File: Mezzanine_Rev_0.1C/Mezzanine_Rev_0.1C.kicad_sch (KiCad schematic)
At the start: 51 parts, among them J1 QBUS_DWK_64Pin_MBT, J2 DIP20 Header, J3 DIP20 Header, J4 IDC-64M, J5 IDC-16M, J6 IDC-20M, J7 Conn_01x03_Pin, J8 Conn_01x07_Pin, U1 1533LI1, U10 74LS07, U11 74LS74, U2 1533TM2, U3 1533LA8, U4 CD74HCT4067M, U5 1533LE4, U6 1533AP6, U7 1533AP6, U8 74LS07, U9 74LS07

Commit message: Mezzanine: Board layout
Completed layout, to be verified and refined if needed.
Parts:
- removed J8: Conn_01x07_Pin, Connector_PinHeader_2.54mm:PinHeader_1x06_P2.54mm_Horizontal, symbol Connector:Conn_01x07_Pin
- added C11, C12, C13, C14, C15, C16, C17, C18, C19, C20: 0.1uF, Capacitor_THT:C_Disc_D6.0mm_W2.5mm_P5.00mm, symbol Device:C
- added unit 2 of DD1
- added unit 2 of DD10
- added unit 2 of DD2
- added unit 2 of DD3
- added unit 2 of DD4
- added unit 2 of DD6
- added unit 2 of DD7
- added unit 2 of DD8
- added unit 2 of DD9
- added J8: Conn_01x16_Pin, Connector_PinHeader_2.54mm:PinHeader_1x16_P2.54mm_Horizontal, symbol Connector:Conn_01x16_Pin
- added R7: 2.2K, Resistor_THT:R_Axial_DIN0204_L3.6mm_D1.6mm_P7.62mm_Horizontal, symbol Device:R
- added unit 7 of U10
- added unit 3 of U11
- added unit 1 of U8
- added unit 2 of U8
- added unit 4 of U8
- added unit 5 of U8
- added unit 6 of U8
- added unit 7 of U8
- added unit 3 of U9
- R6: footprint Resistor_THT:R_Axial_DIN0204_L3.6mm_D1.6mm_P7.62mm_Horizontal -> Resistor_THT:R_Axial_DIN0207_L6.3mm_D2.5mm_P7.62mm_Horizontal
- U4: footprint Package_SO:SOIC-24W_7.5x15.4mm_P1.27mm -> Package_DIP:DIP-24_W15.24mm
- renumbered D6 to DD6, D7 to DD7
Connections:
- net BDCOK: now also RN3.3 (R2); no longer RN3.2 (R1)
- net BPOK: now also RN3.2 (R1); no longer RN2.10 (R9)
- net CPU_DIN: now also J8.12 (Pin_12)
- net DOUT: now also J8.13 (Pin_13)
- net GND: now also C11.2, C12.2, C13.2, C14.2, C15.2, C16.2, C17.2, C18.2, C19.2, C20.2, DD1.8 (GND), DD10.8 (GND), DD2.8 (GND), DD3.8 (GND), DD4.8 (GND), DD6.8 (GND), DD7.8 (GND), DD8.8 (GND), DD9.8 (GND), U10.7 (GND), U11.7 (GND), U8.7 (GND); no longer DD1.8 (GND), DD10.8 (GND), DD2.8 (GND), DD3.8 (GND), DD4.8 (GND), DD6.8 (GND), DD7.8 (GND), DD8.8 (GND), DD9.8 (GND), U10.7 (GND), U8.7 (GND)
- net SEL1: now also J8.14 (Pin_14)
- net SRUN: now also RN4.4 (R3); no longer RN4.8 (R7)
- net SSpare7: now also RN2.8 (R7); no longer RN2.7 (R6)
- net SYSRAM: now also J8.15 (Pin_15)
- net VCC: now also C11.1, C12.1, C13.1, C14.1, C15.1, C16.1, C17.1, C18.1, C19.1, C20.1, DD1.16 (VCC), DD10.16 (VCC), DD2.16 (VCC), DD3.16 (VCC), DD4.16 (VCC), DD6.16 (VCC), DD7.16 (VCC), DD8.16 (VCC), DD9.16 (VCC), R7.1, U10.14 (VCC), U11.14 (VCC), U8.14 (VCC); no longer DD1.16 (VCC), DD10.16 (VCC), DD2.16 (VCC), DD3.16 (VCC), DD4.16 (VCC), DD6.16 (VCC), DD7.16 (VCC), DD8.16 (VCC), DD9.16 (VCC), U10.14 (VCC), U8.14 (VCC)
- net ~{A0}: now also U8.9; no longer U8.1
- net ~{A10}: now also U9.13; no longer U9.11
- net ~{A11}: now also U9.1; no longer U9.13
- net ~{A12}: now also U10.9; no longer U10.1
- net ~{A13}: now also U10.5; no longer U10.3
- net ~{A14}: now also U10.11; no longer U10.5
- net ~{A15}: now also U10.3; no longer U10.9
- net ~{A1}: now also U8.5; no longer U8.3
- net ~{A2}: now also U8.11; no longer U8.5
- net ~{A3}: now also U8.3; no longer U8.9
- net ~{A4}: now also U8.13; no longer U8.11
- net ~{A5}: now also U8.1; no longer U8.13
- net ~{A6}: now also U9.9; no longer U9.1
- net ~{A7}: now also U9.5; no longer U9.3
- net ~{A8}: now also U9.11; no longer U9.5
- net ~{A9}: now also U9.3; no longer U9.9
- net ~{BBS7}: now also RN3.10 (R9); no longer RN3.8 (R7)
- net ~{BDAL0}: now also RN3.5 (R4); no longer RN3.4 (R3)
- net ~{BDAL10}: now also RN1.8 (R7); no longer RN1.7 (R6)
- net ~{BDAL11}: now also RN1.6 (R5)
- net ~{BDAL1}: now also RN3.4 (R3); no longer RN3.3 (R2)
- net ~{BDAL2}: now also RN2.9 (R8); no longer RN2.8 (R7)
- net ~{BDAL3}: now also RN2.7 (R6); no longer RN2.6 (R5)
- net ~{BDAL4}: now also RN2.6 (R5); no longer RN2.5 (R4)
- net ~{BDAL5}: now also RN2.5 (R4); no longer RN2.4 (R3)
- net ~{BDAL6}: now also RN2.4 (R3); no longer RN2.3 (R2)
- net ~{BDAL7}: now also RN2.3 (R2); no longer RN2.2 (R1)
- net ~{BDAL8}: now also RN2.2 (R1); no longer RN1.10 (R9)
- net ~{BDAL9}: now also RN1.9 (R8); no longer RN1.8 (R7)
- net ~{BDIN}: now also RN4.3 (R2); no longer RN4.7 (R6)
- net ~{BDMGI}: now also RN3.8 (R7); no longer RN3.7 (R6)
- net ~{BDMGO}: now also RN3.7 (R6); no longer RN3.6 (R5)
- net ~{BDMR}: now also RN4.10 (R9); no longer RN4.2 (R1)
- net ~{BDOUT}: now also R7.2; no longer RN4.10 (R9)
- net ~{BEVNT}: now also RN1.7 (R6); no longer RN1.6 (R5)
- net ~{BIAKI}: now also RN4.8 (R7); no longer RN4.3 (R2)
- net ~{BIAKO}: now also RN4.9 (R8); no longer RN3.10 (R9)
- net ~{BINIT}: now also RN3.6 (R5); no longer RN3.5 (R4)
- net ~{BIRQ3}: now also RN2.10 (R9); no longer RN2.9 (R8)
- net ~{BIRQ4}: now also RN4.7 (R6); no longer RN4.4 (R3)
- net ~{BRPLY}: now also RN4.2 (R1); no longer RN4.9 (R8)
- net ~{BSACK}: now also RN1.10 (R9); no longer RN1.9 (R8)
- net ~{BSYNC}: now also RN4.5 (R4); no longer RN4.6 (R5)
- net ~{BWTBT}: now also RN4.6 (R5); no longer RN4.5 (R4)
- net ~{CPU_DIN}: now also J8.11 (Pin_11)
- net ~{CPU_DOUT}: now also J8.8 (Pin_8)
- net ~{CPU_RPLY}: now also J8.4 (Pin_4)
- net ~{EXT_DMG}: now also J8.10 (Pin_10)
- net ~{EXT_IRQ2}: now also J8.6 (Pin_6)
- net ~{EXT_SYNC}: now also J8.9 (Pin_9)
- net ~{EXT_VIRQ}: now also J8.3 (Pin_3)
- net ~{EXT_WTBT}: now also J8.7 (Pin_7)
- net ~{IA0}: now also U8.8; no longer U8.2
- net ~{IA10}: now also U9.12; no longer U9.10
- net ~{IA11}: now also U9.2; no longer U9.12
- net ~{IA12}: now also U10.8; no longer U10.2
- net ~{IA13}: now also U10.6; no longer U10.4
- net ~{IA14}: now also U10.10; no longer U10.6
- net ~{IA15}: now also U10.4; no longer U10.8
- net ~{IA1}: now also U8.6; no longer U8.4
- net ~{IA2}: now also U8.10; no longer U8.6
- net ~{IA3}: now also U8.4; no longer U8.8
- net ~{IA4}: now also U8.12; no longer U8.10
- net ~{IA5}: now also U8.2; no longer U8.12
- net ~{IA6}: now also U9.8; no longer U9.2
- net ~{IA7}: now also U9.6; no longer U9.4
- net ~{IA8}: now also U9.10; no longer U9.6
- net ~{IA9}: now also U9.4; no longer U9.8
- net ~{LOCK}: now also J8.16 (Pin_16)
- net ~{M2}: now also U10.13; no longer U10.11
- net ~{M3}: now also U10.1; no longer U10.13
- net ~{ROM_DIN}: now also J8.5 (Pin_5)
- net at U11.5 (Q): now also J8.1 (Pin_1)
- net at U11.6 (~{Q}): now also J8.2 (Pin_2)
- net at J6.17 (Pin_17): now also U10.12; no longer U10.10
- net at J6.19 (Pin_19): now also U10.2; no longer U10.12
- new net: R4.2, U11.10 (~{S}), U11.11 (C), U11.12 (D), U11.13 (~{R}), U11.2 (D), U11.3 (C)
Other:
- moved on the sheet: C1, C10, C2, C3, C4, C5, C6, C7, C8, C9, DD1A, DD2A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

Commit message: Mezzanine: Improve layout
More power connections, rearranged resistors.
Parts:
- added unit 3 of U11
- R6: footprint Resistor_THT:R_Axial_DIN0207_L6.3mm_D2.5mm_P7.62mm_Horizontal -> Resistor_THT:R_Axial_DIN0204_L3.6mm_D1.6mm_P7.62mm_Horizontal
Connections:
- net GND: now also U11.7 (GND); no longer U11.7 (GND)
- net VCC: now also U11.14 (VCC); no longer U11.14 (VCC)
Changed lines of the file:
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@@
 			)
 		)
-		(property "Footprint" "Resistor_THT:R_Axial_DIN0207_L6.3mm_D2.5mm_P7.62mm_Horizontal"
+		(property "Footprint" "Resistor_THT:R_Axial_DIN0204_L3.6mm_D1.6mm_P7.62mm_Horizontal"
 			(at 60.452 147.32 90)
 			(hide yes)

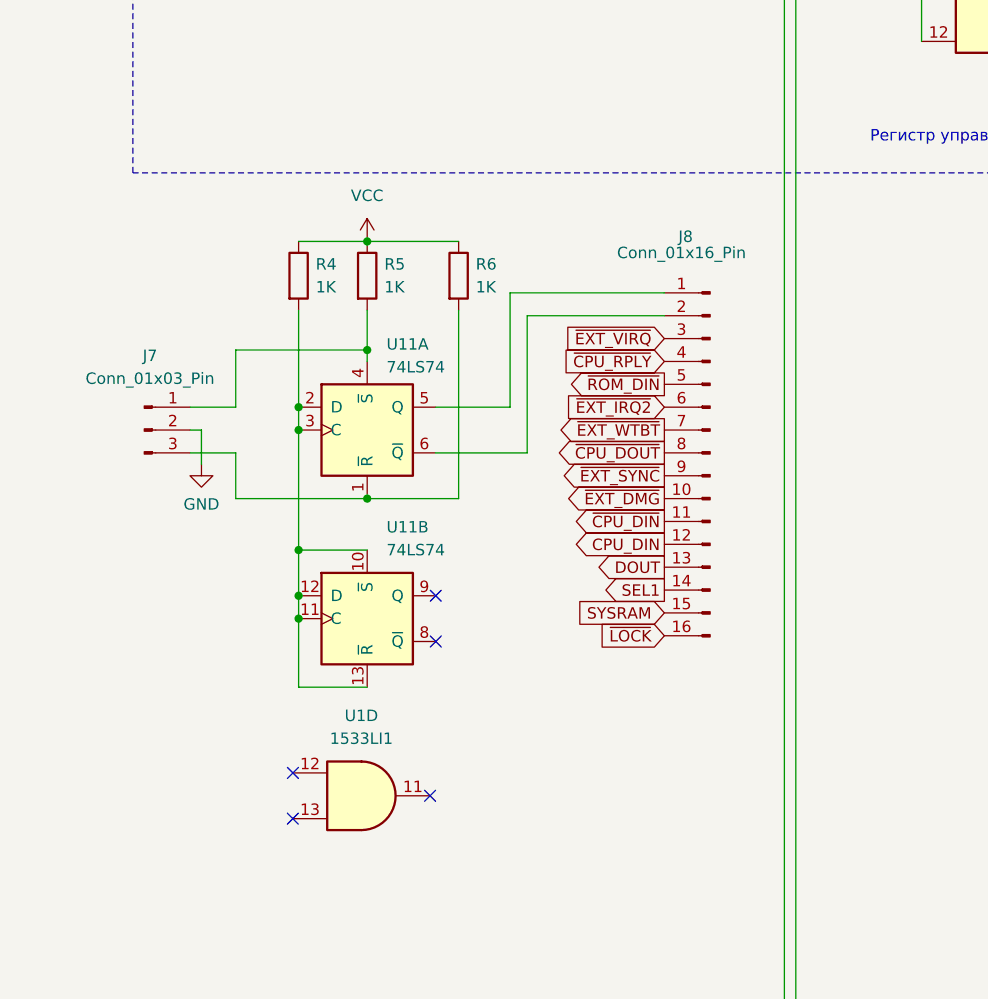
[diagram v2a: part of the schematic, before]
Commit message: Mezzanine: Change J8
Use dual-row angular connector, actually possible to use IDC-16. Gives way to
main board's oscillator and also allows for crimping on the cable.
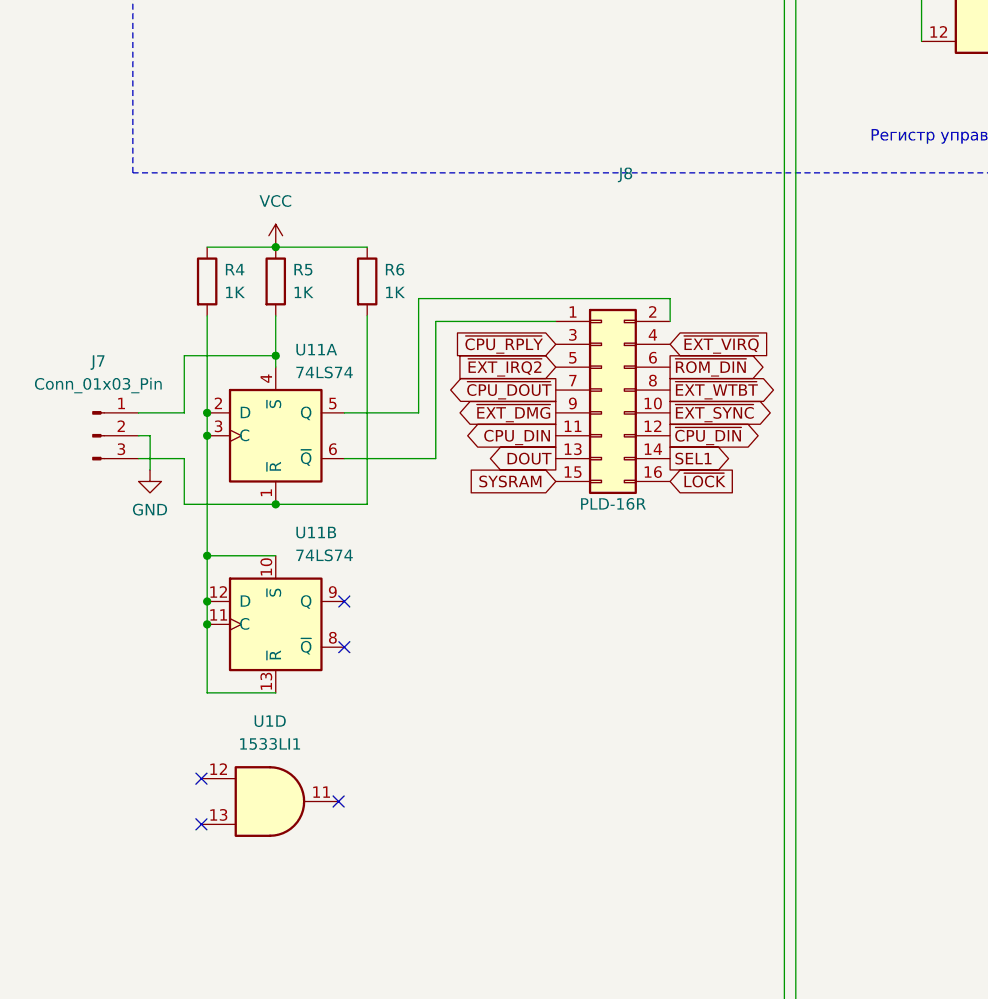
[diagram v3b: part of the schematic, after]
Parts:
- removed J8: Conn_01x16_Pin, Connector_PinHeader_2.54mm:PinHeader_1x16_P2.54mm_Horizontal, symbol Connector:Conn_01x16_Pin
- added J8: PLD-16R, Connector_PinHeader_2.54mm:PinHeader_2x08_P2.54mm_Horizontal, symbol Connector_Generic:Conn_02x08_Odd_Even
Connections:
- net CPU_DIN: now also J8.11 (Pin_11)
- net DOUT: now also J8.13 (Pin_13)
- net SEL1: now also J8.14 (Pin_14)
- net SYSRAM: now also J8.15 (Pin_15)
- net ~{CPU_DIN}: now also J8.12 (Pin_12)
- net ~{CPU_DOUT}: now also J8.7 (Pin_7)
- net ~{CPU_RPLY}: now also J8.3 (Pin_3)
- net ~{EXT_DMG}: now also J8.9 (Pin_9)
- net ~{EXT_IRQ2}: now also J8.5 (Pin_5)
- net ~{EXT_SYNC}: now also J8.10 (Pin_10)
- net ~{EXT_VIRQ}: now also J8.4 (Pin_4)
- net ~{EXT_WTBT}: now also J8.8 (Pin_8)
- net ~{LOCK}: now also J8.16 (Pin_16)
- net ~{ROM_DIN}: now also J8.6 (Pin_6)
- net at U11.5 (Q): now also J8.2 (Pin_2)
- net at U11.6 (~{Q}): now also J8.1 (Pin_1)
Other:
- moved on the sheet: J7, R4, R5, R6, U11A, U11B, U1D

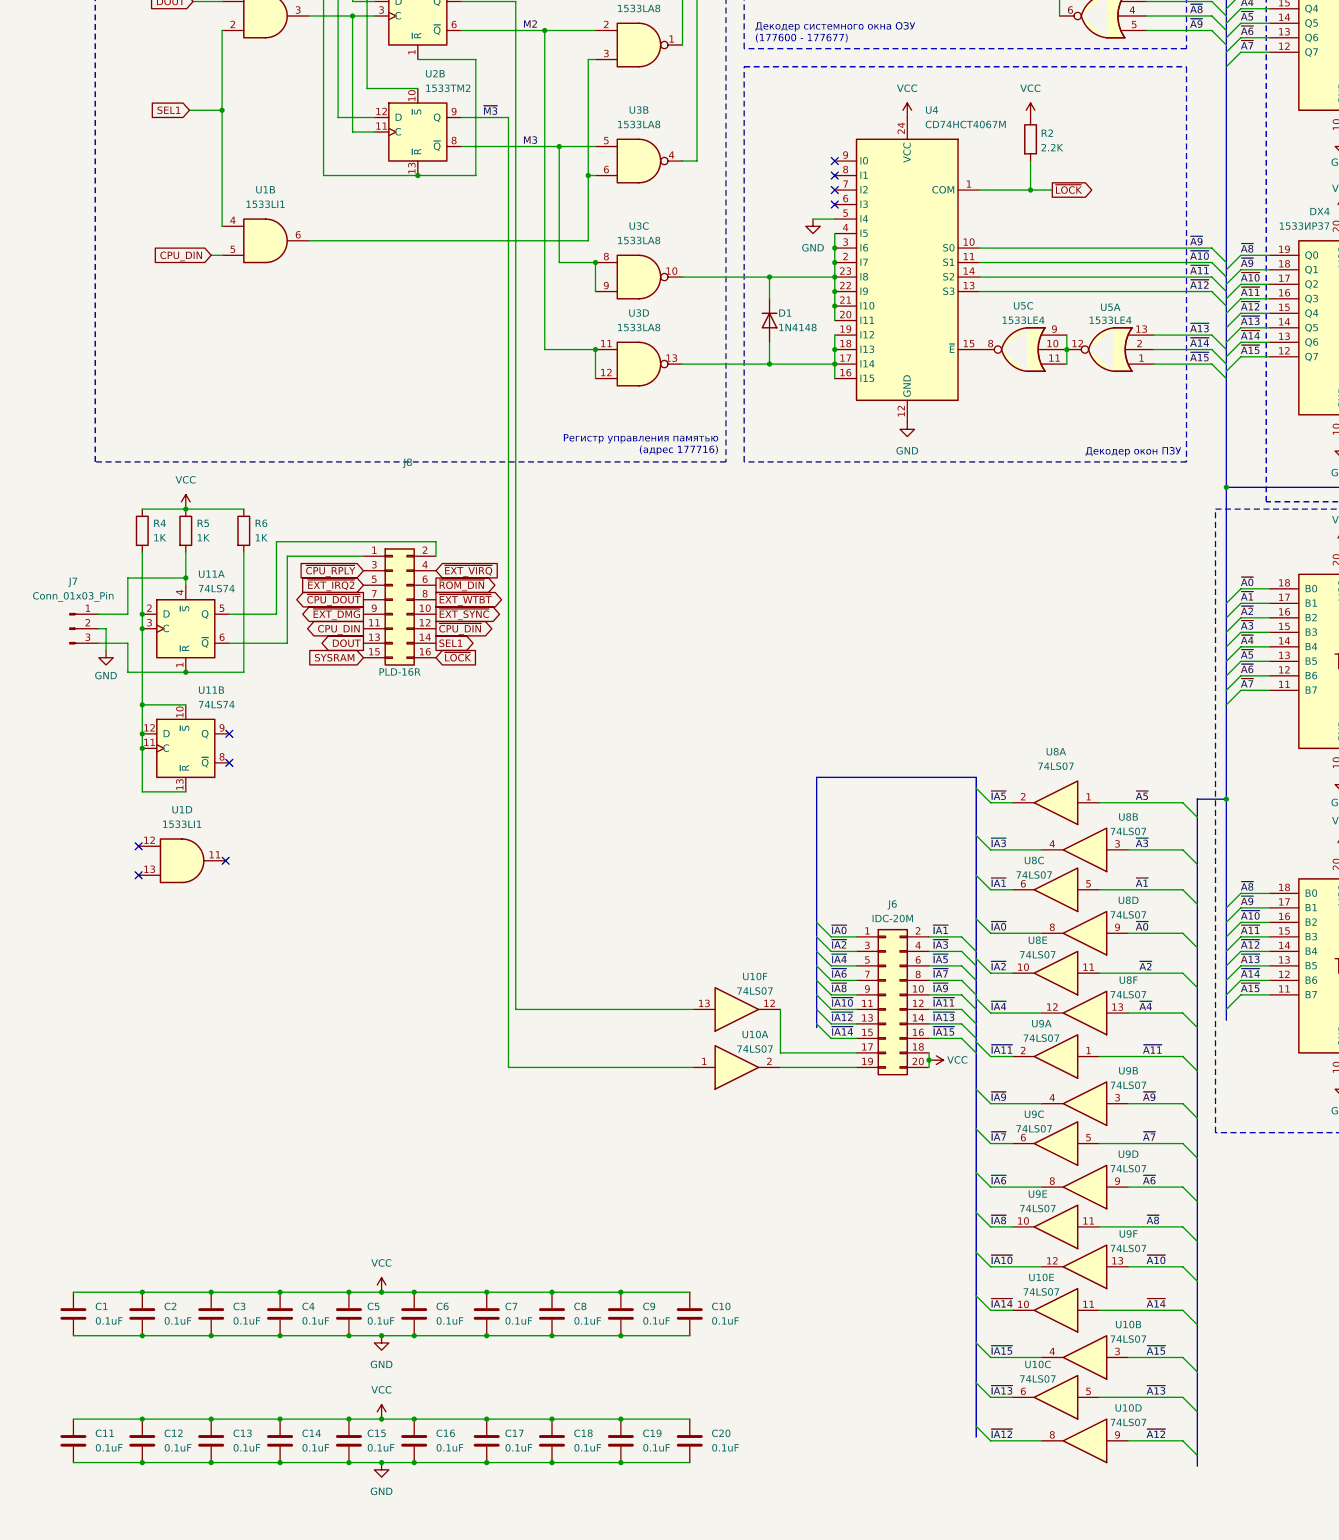
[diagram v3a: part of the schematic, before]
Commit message: Mezzanine: SOIC option for U4
DIP version is rare, let's give another option.
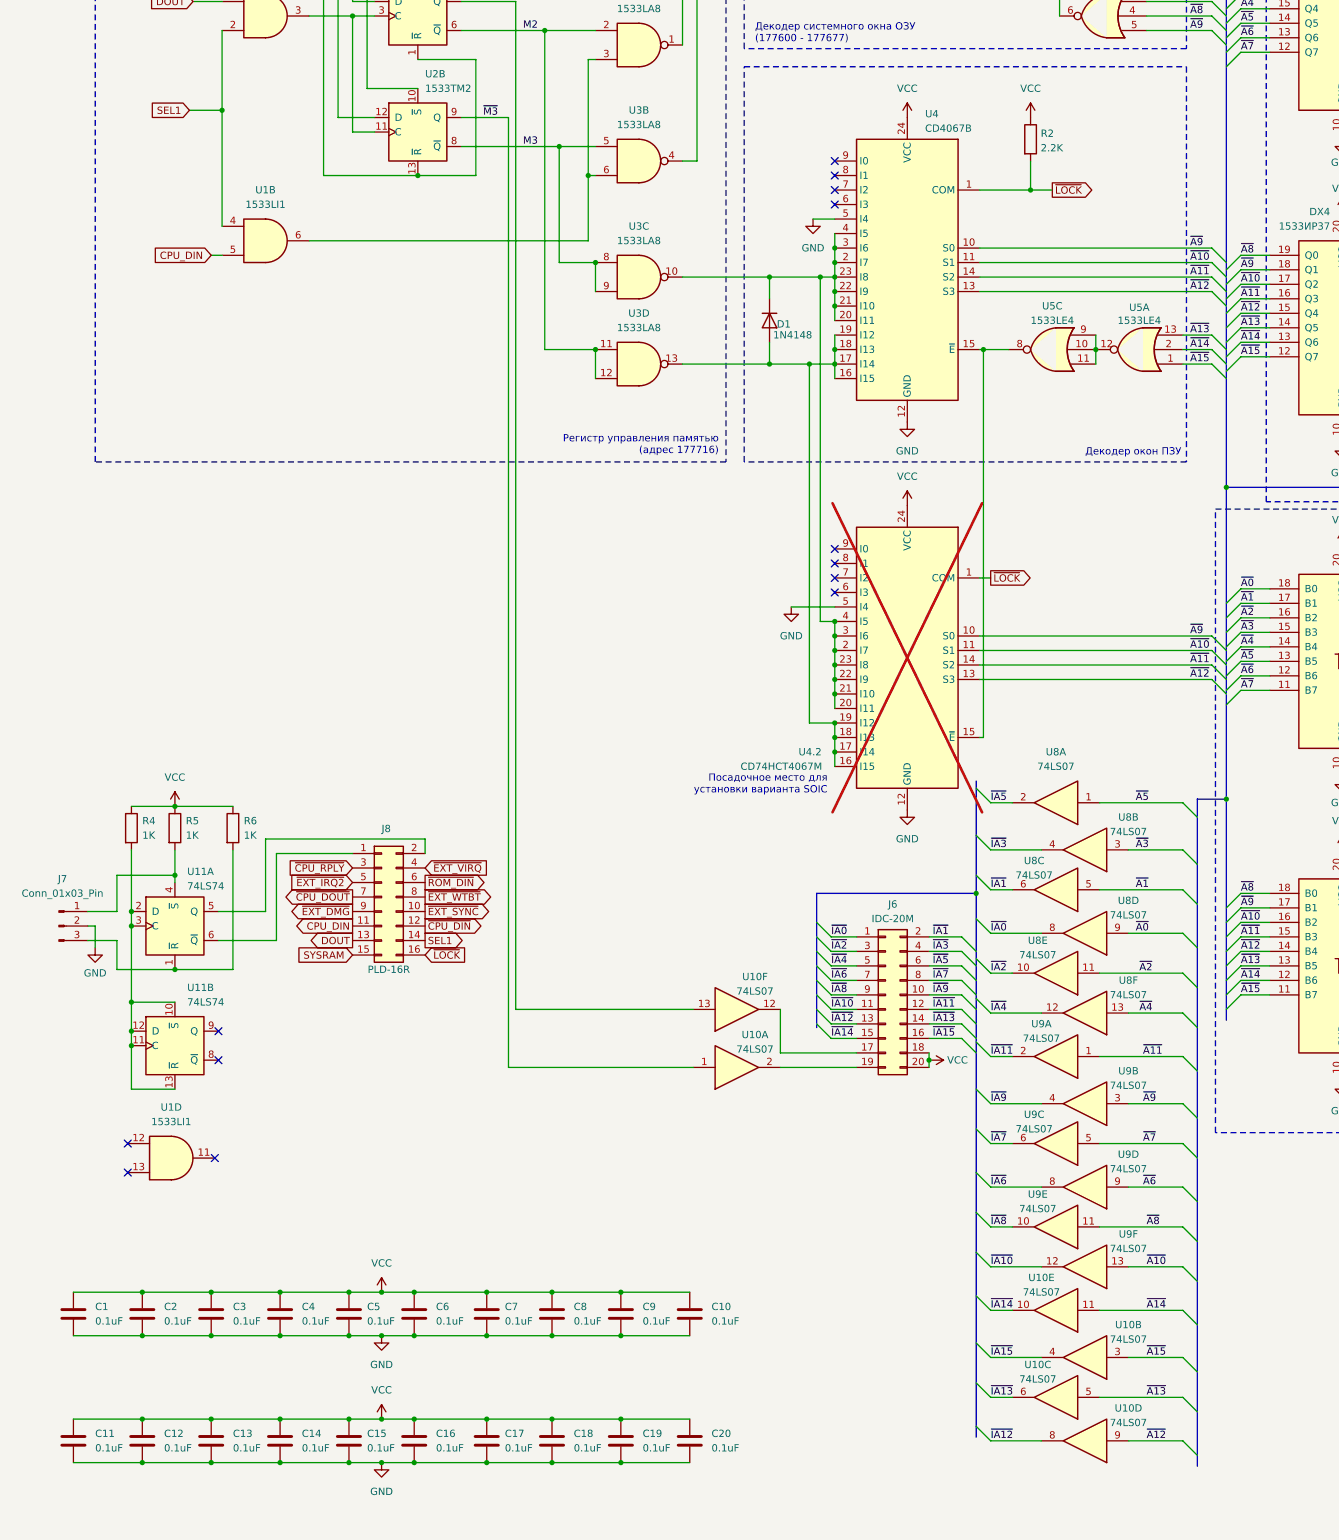
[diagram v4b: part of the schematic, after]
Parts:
- added U4.2: CD74HCT4067M, Package_SO:SOIC-24W_7.5x15.4mm_P1.27mm, symbol 74xx:CD74HC4067M
- U4: value CD74HCT4067M -> CD4067B
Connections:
- net GND: now also U4.2.12 (GND), U4.2.5 (I4)
- net VCC: now also U4.2.24 (VCC)
- net ~{A10}: now also U4.2.11 (S1)
- net ~{A11}: now also U4.2.14 (S2)
- net ~{A12}: now also U4.2.13 (S3)
- net ~{A9}: now also U4.2.10 (S0)
- net ~{LOCK}: now also U4.2.1 (COM)
- net at D1.1 (K), U3.10, U4.2 (I7)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: now also U4.2.2 (I7), U4.2.20 (I11), U4.2.21 (I10), U4.2.22 (I9), U4.2.23 (I8), U4.2.3 (I6), U4.2.4 (I5)
- net at D1.2 (A), U3.13, U4.16 (I15)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: now also U4.2.16 (I15), U4.2.17 (I14), U4.2.18 (I13), U4.2.19 (I12)
- net at U4.15 (~{E}), U5.8: now also U4.2.15 (~{E})
- no-connect marks 38 -> 42
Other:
- note added: "Посадочное место для установки варианта SOIC"
- moved on the sheet: J7, J8, R4, R5, R6, U11A, U11B, U1D, U5A, U5C
